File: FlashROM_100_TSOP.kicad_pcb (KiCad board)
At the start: 2 copper layers, 16.5 x 34.3 mm, 7 parts, among them J1 LH535618 DIP LEGS, U1 29F010

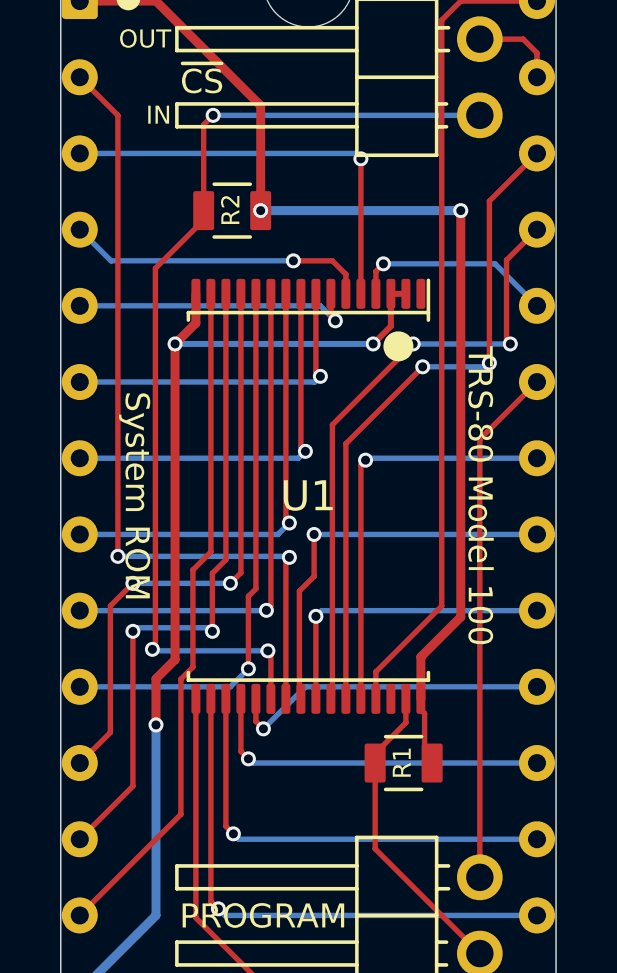
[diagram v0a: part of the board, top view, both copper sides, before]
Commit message: add model 100 optrom programming adapter. readme and renders
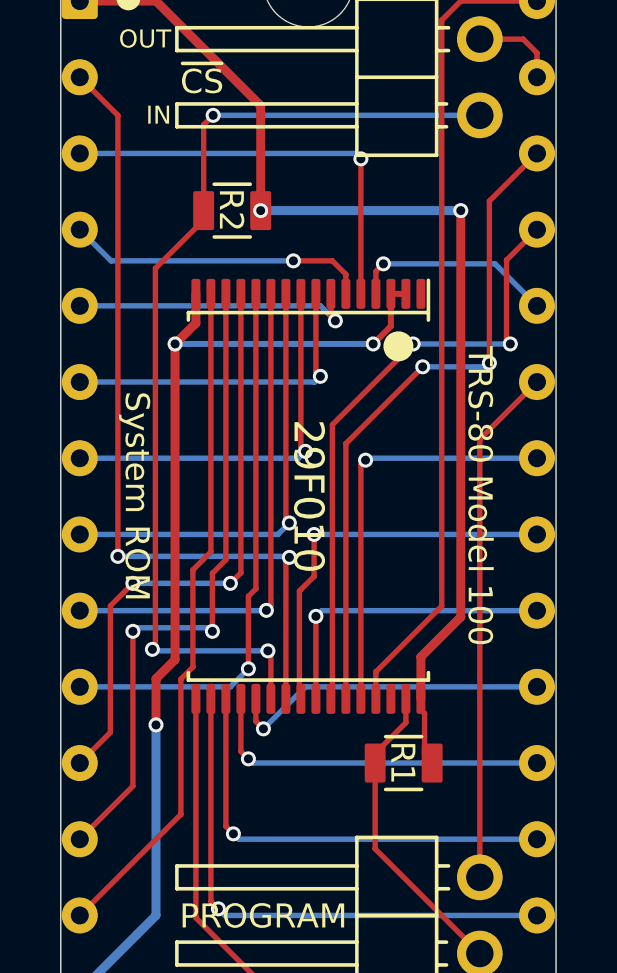
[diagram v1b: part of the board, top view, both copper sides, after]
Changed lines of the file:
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@@
-(kicad_pcb (version 20171130) (host pcbnew 5.1.9-73d0e3b20d~88~ubuntu20.10.1)
+(kicad_pcb (version 20171130) (host pcbnew 5.1.10-88a1d61d58~88~ubuntu20.10.1)
   (general
     (thickness 1.6)
@@
   (title_block
     (title FlashROM_100)
-    (date 2021-03-07)
-    (rev 002)
+    (date 2021-05-12)
+    (rev 003)
     (company "Brian K. White - b.kenyon.w@gmail.com")
     (comment 1 "System ROM for TRS-80 Model 100 with support for REX main rom feature")
@@
     (visible_elements FFFFFF7F)
     (pcbplotparams
-      (layerselection 0x010fc_ffffffff)
+      (layerselection 0x010f0_ffffffff)
       (usegerberextensions false)
       (usegerberattributes false)
@@
     (tags "CMS TSOP")
     (attr smd)
-    (fp_text reference U1 (at 0 0 unlocked) (layer F.SilkS)
-      (effects (font (size 1 1) (thickness 0.15)))
-    )
-    (fp_text value 29F010 (at 1.27 0 90) (layer F.Fab)
+    (fp_text reference U1 (at 0 0 unlocked) (layer F.SilkS) hide
+      (effects (font (size 1 1) (thickness 0.15)))
+    )
+    (fp_text value 29F010 (at 0 0 270 unlocked) (layer F.SilkS)
       (effects (font (size 1 1) (thickness 0.15)))
     )
@@
     (tags "resistor 0805")
     (attr smd)
-    (fp_text reference R1 (at -0.04 -0.01 -270 unlocked) (layer F.SilkS)
-      (effects (font (size 0.6 0.6) (thickness 0.08)))
+    (fp_text reference R1 (at -0.04 -0.01 -90 unlocked) (layer F.SilkS)
+      (effects (font (size 0.8 0.8) (thickness 0.1)))
     )
     (fp_text value 47K (at 0 1.75) (layer F.Fab) hide
@@
     (tags "resistor 0805")
     (attr smd)
-    (fp_text reference R2 (at -0.04 -0.02 90 unlocked) (layer F.SilkS)
-      (effects (font (size 0.6 0.6) (thickness 0.08)))
+    (fp_text reference R2 (at -0.04 -0.02 -90 unlocked) (layer F.SilkS)
+      (effects (font (size 0.8 0.8) (thickness 0.1)))
     )
     (fp_text value 47K (at 0 1.75) (layer F.Fab)

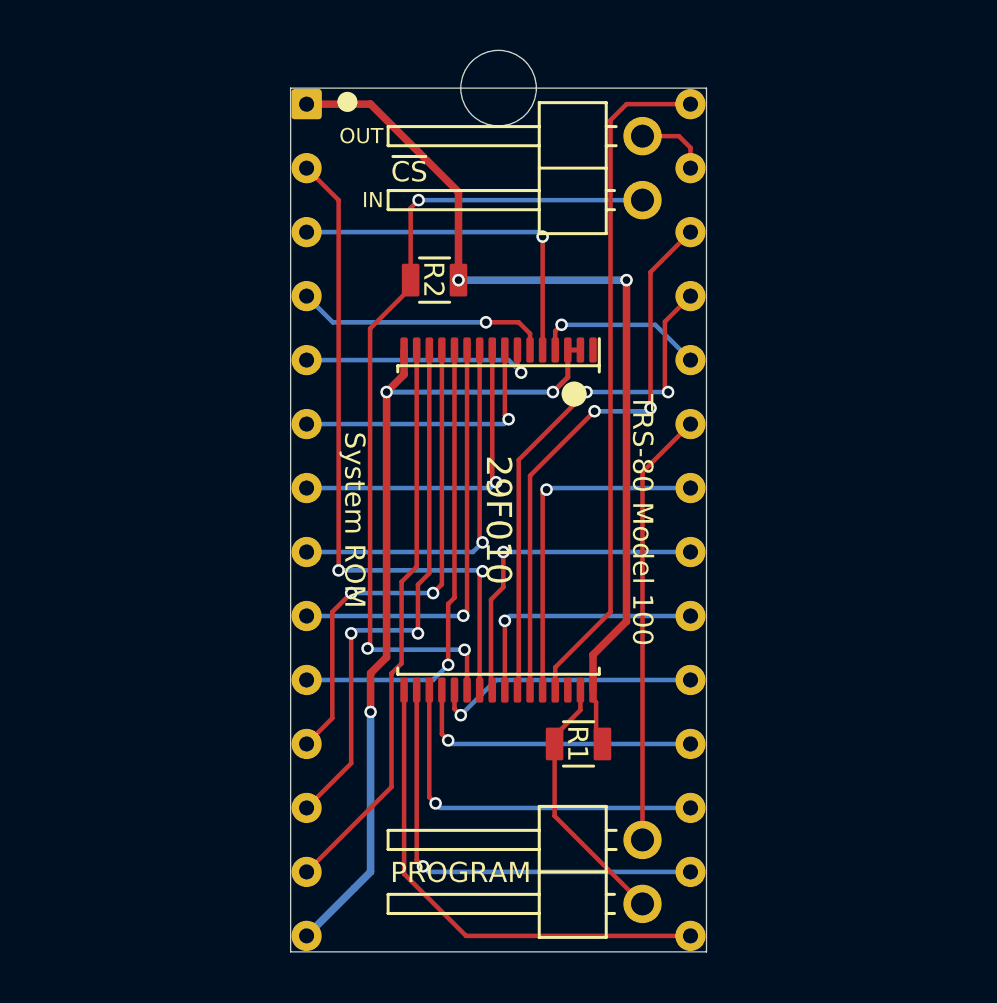
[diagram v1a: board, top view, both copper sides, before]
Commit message: add DS1000_DIP14
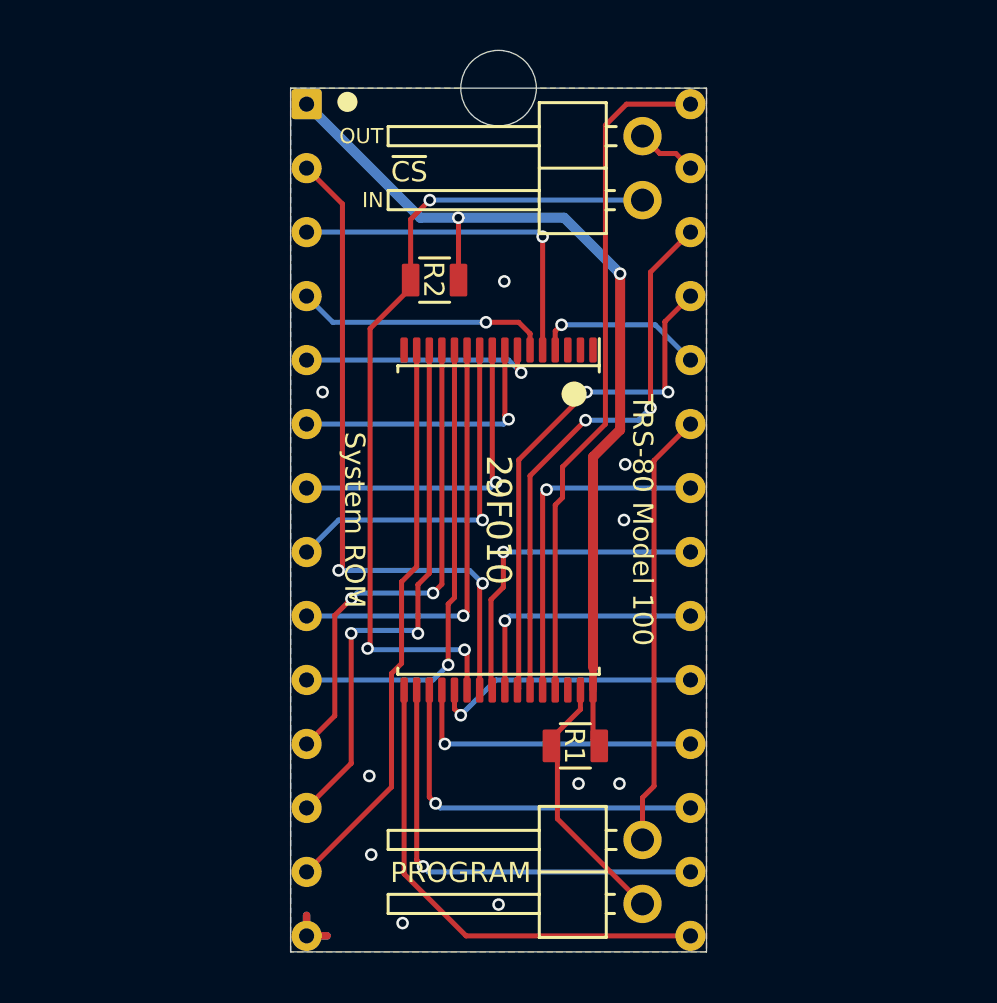
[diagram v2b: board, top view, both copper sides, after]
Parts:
- moved R1 0.15 mm to (153.0, 109.0)
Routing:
- net GND: track 33.9 -> 3.25 mm, vias 3 -> 10
- net /A2: track 14.8 -> 14.3 mm
- added copper zone on B.Cu, net GND
- added copper zone on F.Cu, net GND
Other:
- net class Default: clearance 0.16 -> 0.2; trace_width 0.18 -> 0.2
- rule trace_clearance: 0.16 -> 0.2
- rule trace_min: 0.16 -> 0.2

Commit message: kicad 6
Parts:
- JP1: value ~CS~ breakout -> ~{CS} breakout
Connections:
- net /ALE_~WE renamed /ALE_~{WE}
- net /~CS renamed /~{CS}
- net /~CS_BUS renamed /~{CS_BUS}
- net /~OE renamed /~{OE}
- net /~WE renamed /~{WE}
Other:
- net class Default removed
- board text added: "Connect ~{CS} OUT to REX TP1. Leave ~{CS} IN unconnected."
- board text added: "If REX is later removed, connect ~{CS} OUT to ~{CS} IN."
- board text added: "Install a shunt on ~{CS}, or, install wires as above,"
- board text added: "Run 2 wires from ~{CS} IN & ~{CS} OUT to Option ROM compartment."
- board text added: "~{CS}"
- board text removed: "Connect ~CS~ OUT to REX TP1. Leave ~CS~ IN unconnected."
- board text removed: "If REX is later removed, connect ~CS~ OUT to ~CS~ IN."
- board text removed: "Install a shunt on ~CS~, or, install wires as above,"
- board text removed: "Run 2 wires from ~CS~ IN & ~CS~ OUT to Option ROM compartment."
- board text removed: "~CS"

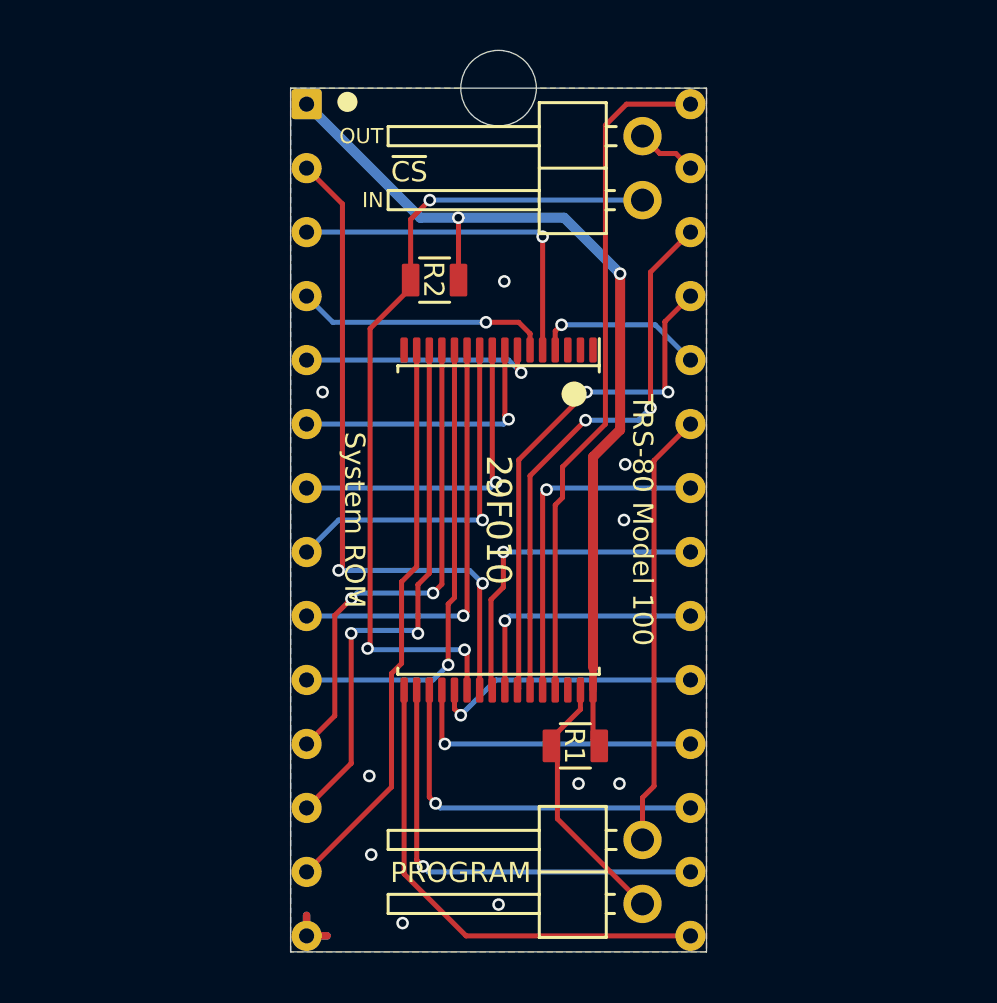
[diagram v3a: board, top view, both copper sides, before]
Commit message: Fix wrong pinout on FlashROM_100 TSOPgit add -A!
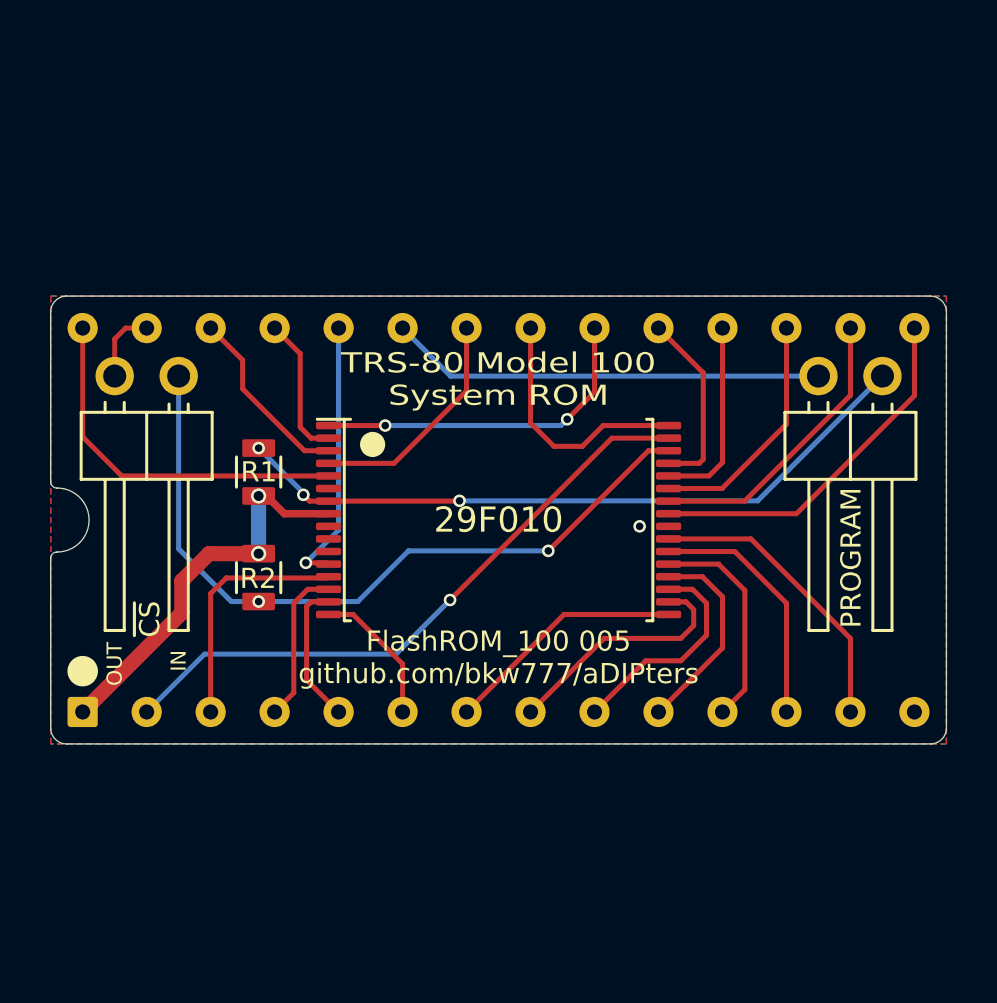
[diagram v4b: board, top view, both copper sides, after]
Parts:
- removed REF**: NPTH_3mm, 000_LOCAL:NPTH_3mm
- J1: footprint 000_LOCAL:DIP28_0.6_pcb_sil_pins -> 000_LOCAL:DIP28_0.6_pcb
- JP1: value ~{CS} breakout -> ~CS~ breakout
- moved JP2 23.0 mm to (165.2, 94.3), turned to -90 degrees
- moved JP1 19.7 mm to (137.3, 94.3), turned to -90 degrees
- moved R1 16.6 mm to (140.5, 98.1), turned to -90 degrees
- moved R2 13.7 mm to (140.5, 102.3), turned to 90 degrees
- turned J1 to 90 degrees
- turned U1 to -90 degrees
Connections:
- U1 pad 1: (no net) -> /A11
- U1 pad 10: /A2 -> GND
- U1 pad 11: /A1 -> GND
- U1 pad 12: /A0 -> /A12
- U1 pad 13: /D0 -> /A7
- U1 pad 14: /D1 -> /A6
- U1 pad 15: /D2 -> /A5
- U1 pad 16: GND -> /A4
- U1 pad 17: /D3 -> /A3
- U1 pad 18: /D4 -> /A2
- U1 pad 19: /D5 -> /A1
- U1 pad 2: GND -> /A9
- U1 pad 20: /D6 -> /A0
- U1 pad 21: /D7 -> /D0
- U1 pad 22: /~{CS} -> /D1
- U1 pad 23: /A10 -> /D2
- U1 pad 24: /~{OE} -> GND
- U1 pad 25: /A11 -> /D3
- U1 pad 26: /A9 -> /D4
- U1 pad 27: /A8 -> /D5
- U1 pad 28: /A13 -> /D6
- U1 pad 29: /A14 -> /D7
- U1 pad 3: GND -> /A8
- U1 pad 30: (no net) -> /~{CS}
- U1 pad 31: /~{WE} -> /A10
- U1 pad 32: VCC -> /~{OE}
- U1 pad 4: /A12 -> /A13
- U1 pad 5: /A7 -> /A14
- U1 pad 6: /A6 -> unconnected-(U1-Pad6)
- U1 pad 7: /A5 -> /~{WE}
- U1 pad 8: /A4 -> VCC
- U1 pad 9: /A3 -> unconnected-(U1-Pad9)
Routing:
- net VCC: track 37.0 -> 15.7 mm
- net /~{WE}: track 10.5 -> 27.7 mm, vias 0 -> 3
- net /A9: track 20.5 -> 5.66 mm, vias 2 -> 0
- net /A8: track 22.0 -> 7.37 mm, vias 2 -> 0
- net /A14: track 27.0 -> 14.7 mm
- net /D1: track 21.8 -> 9.85 mm, vias 2 -> 0
- net /D0: track 19.6 -> 8.66 mm, vias 2 -> 0
- net /D2: track 22.5 -> 11.8 mm
- net /A0: track 18.5 -> 8.09 mm, vias 1 -> 0
- net /A1: track 16.8 -> 8.71 mm, vias 1 -> 0
- net /D4: track 17.8 -> 11.6 mm, vias 1 -> 0
- net /D3: track 19.7 -> 14.4 mm
- net /A4: track 10.9 -> 5.66 mm, vias 1 -> 0
- net /D5: track 14.8 -> 9.55 mm, vias 1 -> 0
- net /A2: track 14.3 -> 9.66 mm, vias 1 -> 0
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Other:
- board size 16.5 x 34.3 mm -> 35.6 x 17.8 mm
- board text added: "${TITLE} ${REVISION} ${COMMENT2}"
- board text added: "R1, R2: ${00000000-0000-0000-0000-0000604ac043:VALUE} Legs: TE 1544210"
- board text added: "REX Main ROM Support: ~{CS} OUT to REX TP1 -> Main ROM from REX ~{CS} OUT to ~{CS} IN -> Main ROM from this board Run 2 wires from ~{CS} to Option ROM bay to allow switching between REX and internal main ROM."
- board text added: "TRS-80 Model 100 System ROM"
- board text removed: "Connect ~{CS} OUT to REX TP1. Leave ~{CS} IN unconnected."
- board text removed: "If REX is later removed, connect ~{CS} OUT to ~{CS} IN."
- board text removed: "Install a shunt on ~{CS}, or, install wires as above,"
- board text removed: "Legs: TE 1544210"
- board text removed: "R1, R2: 47k"
- board text removed: "REX can then be added later without disassembling."
- board text removed: "Run 2 wires from ~{CS} IN & ~{CS} OUT to Option ROM compartment."
- board text removed: "System ROM"
- board text removed: "TRS-80 Model 100"
- board text removed: "To use REX Main ROM feature:"
- board text removed: "To use without REX:"
- board text removed: "and connect them to each other in the Option ROM compartment."

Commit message: dual tsop footprint on flashrom_100
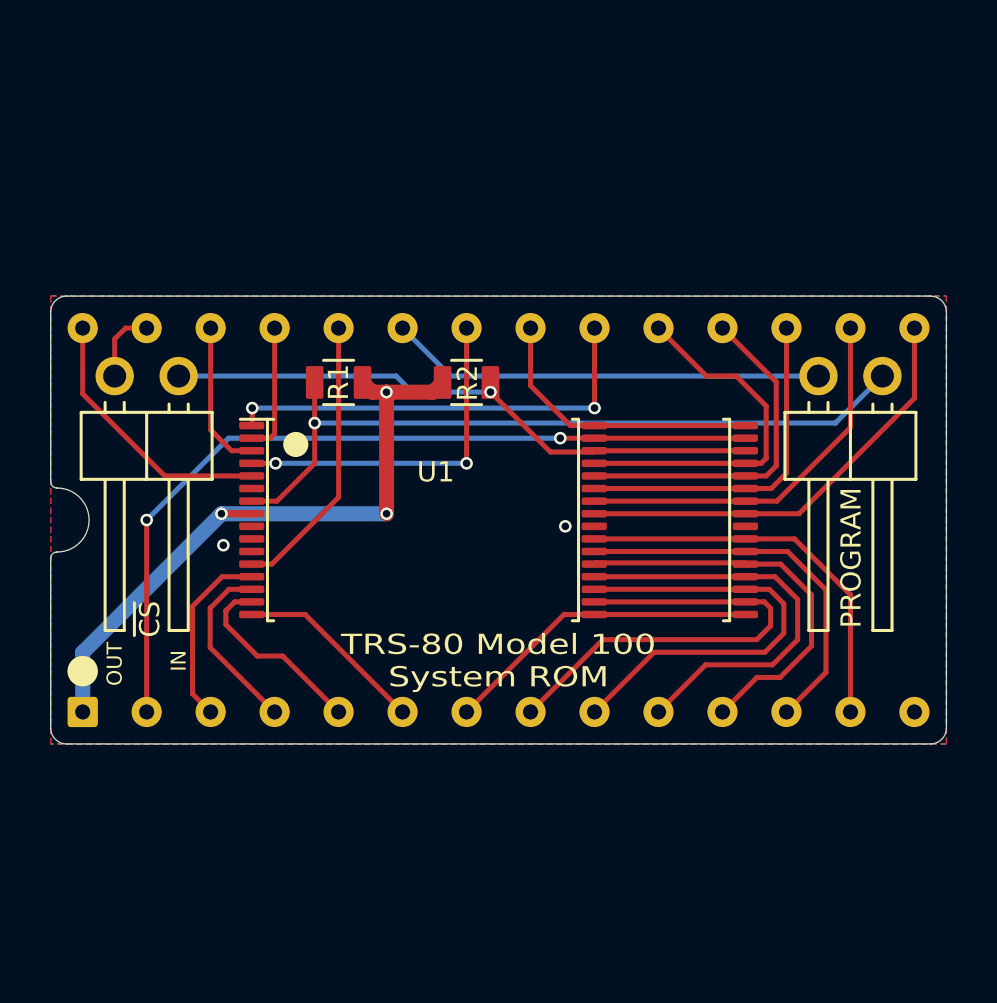
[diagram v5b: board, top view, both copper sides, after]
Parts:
- U1: footprint 000_LOCAL:TSOP32-14mm -> 000_LOCAL:TSOP32-dual
- moved R2 11.3 mm to (148.7, 94.5), turned to 180 degrees
- moved R1 4.77 mm to (143.7, 94.5), turned to 0 degrees
- turned U1 to 0 degrees
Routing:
- net VCC: track 15.7 -> 26.2 mm, vias 2 -> 3
- net /A2: track 9.66 -> 18.9 mm
- net /A1: track 8.71 -> 17.7 mm
- net /A0: track 8.09 -> 16.8 mm
- net /A10: track 25.2 -> 32.7 mm, vias 1 -> 2
- net /D0: track 8.66 -> 15.8 mm
- net /D7: track 7.39 -> 14.5 mm
- net /D6: track 7.70 -> 13.7 mm
- net /~{CS}: track 29.7 -> 24.2 mm, vias 2 -> 1
- net /D1: track 9.85 -> 15.3 mm
- net /A13: track 9.16 -> 13.9 mm, vias 0 -> 2
- net /D5: track 9.55 -> 13.6 mm
- net /A14: track 14.7 -> 10.7 mm
- net /D2: track 11.8 -> 15.7 mm
- net /A11: track 13.6 -> 17.5 mm
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
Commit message: various minor cleanups
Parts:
- JP1: value ~CS~ breakout -> ~{CS} breakout
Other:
- board text added: "REX_Classic main ROM support: ~{CS}_OUT to REX TP1 to boot REX main rom ~{CS}_OUT to ~{CS}_IN to boot internal main rom"
- board text removed: "REX Main ROM Support: ~{CS} OUT to REX TP1 -> Main ROM from REX ~{CS} OUT to ~{CS} IN -> Main ROM from this board Run 2 wires from ~{CS} to Option ROM bay to allow switching between REX and internal main ROM."
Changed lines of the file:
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@@
     (title "FlashROM_100")
     (date "2022-10-12")
-    (rev "006")
+    (rev "tsop_006")
     (company "Brian K. White - b.kenyon.w@gmail.com")
     (comment 1 "System ROM for TRS-80 Model 100 with support for REX main rom feature")
@@
     (property "Sheetname" "")
     (attr smd)
-    (fp_text reference "U1" (at -2.492 -1.905) (layer "F.SilkS")
+    (fp_text reference "U1" (at -3.175 -1.905) (layer "F.SilkS")
       (effects (font (size 0.8 0.8) (thickness 0.1)))
     )
-    (fp_text value "29F010" (at -3 1.27) (layer "F.Fab")
+    (fp_text value "29F010" (at -3 1.27) (layer "F.SilkS")
       (effects (font (size 1 1) (thickness 0.15)))
     )
@@
       (effects (font (size 1 1) (thickness 0.15)))
     )
-    (fp_text value "~CS~ breakout" (at 4.385 4.81 -270) (layer "F.Fab")
+    (fp_text value "~{CS} breakout" (at 4.385 4.81 -270) (layer "F.Fab")
       (effects (font (size 1 1) (thickness 0.15)))
     )
@@
   )
   (gr_circle (center 133.49 106) (end 134.09 106) (layer "F.SilkS") (width 0.01) (fill solid))
-  (gr_text "R1, R2: ${00000000-0000-0000-0000-0000604ac043:VALUE}\nLegs: TE 1544210" (at 167.145 105.461) (layer "B.SilkS")
+  (gr_text "R1, R2: ${00000000-0000-0000-0000-0000604ac043:VALUE}\nLegs: TE 1544210" (at 166.51 105.08) (layer "B.SilkS")
     (effects (font (size 0.6 0.6) (thickness 0.08)) (justify left mirror))
   )
-  (gr_text "REX Main ROM Support:\n~{CS} OUT to REX TP1 -> Main ROM from REX\n~{CS} OUT to ~{CS} IN -> Main ROM from this board\nRun 2 wires from ~{CS} to Option ROM bay to allow\nswitching between REX and internal main ROM." (at 165.875 100) (layer "B.SilkS")
+  (gr_text "REX_Classic main ROM support:\n~{CS}_OUT to REX TP1 to boot REX main rom\n~{CS}_OUT to ~{CS}_IN to boot internal main rom\n" (at 165.875 100) (layer "B.SilkS")
     (effects (font (size 0.8 0.8) (thickness 0.1)) (justify left mirror))
   )
@@
     (effects (font (size 1 1) (thickness 0.15)) (justify mirror))
   )
-  (gr_text "${TITLE} ${REVISION}\n${COMMENT2}" (at 142.38 105.08) (layer "B.SilkS")
+  (gr_text "${TITLE} ${REVISION}\n${COMMENT2}" (at 142.38 104.445) (layer "B.SilkS")
     (effects (font (size 0.8 0.8) (thickness 0.1)) (justify mirror))
   )
